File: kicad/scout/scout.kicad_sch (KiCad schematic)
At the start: 35 parts, among them J1 AudioJack2_SwitchT, J2 Conn_01x06_Male, J3 DIN5, J4 DIN5, SW26 SW_SPST, U1 ATmega328P-PU, U2 LM386, U3 6N138, Y1 16.00MHz

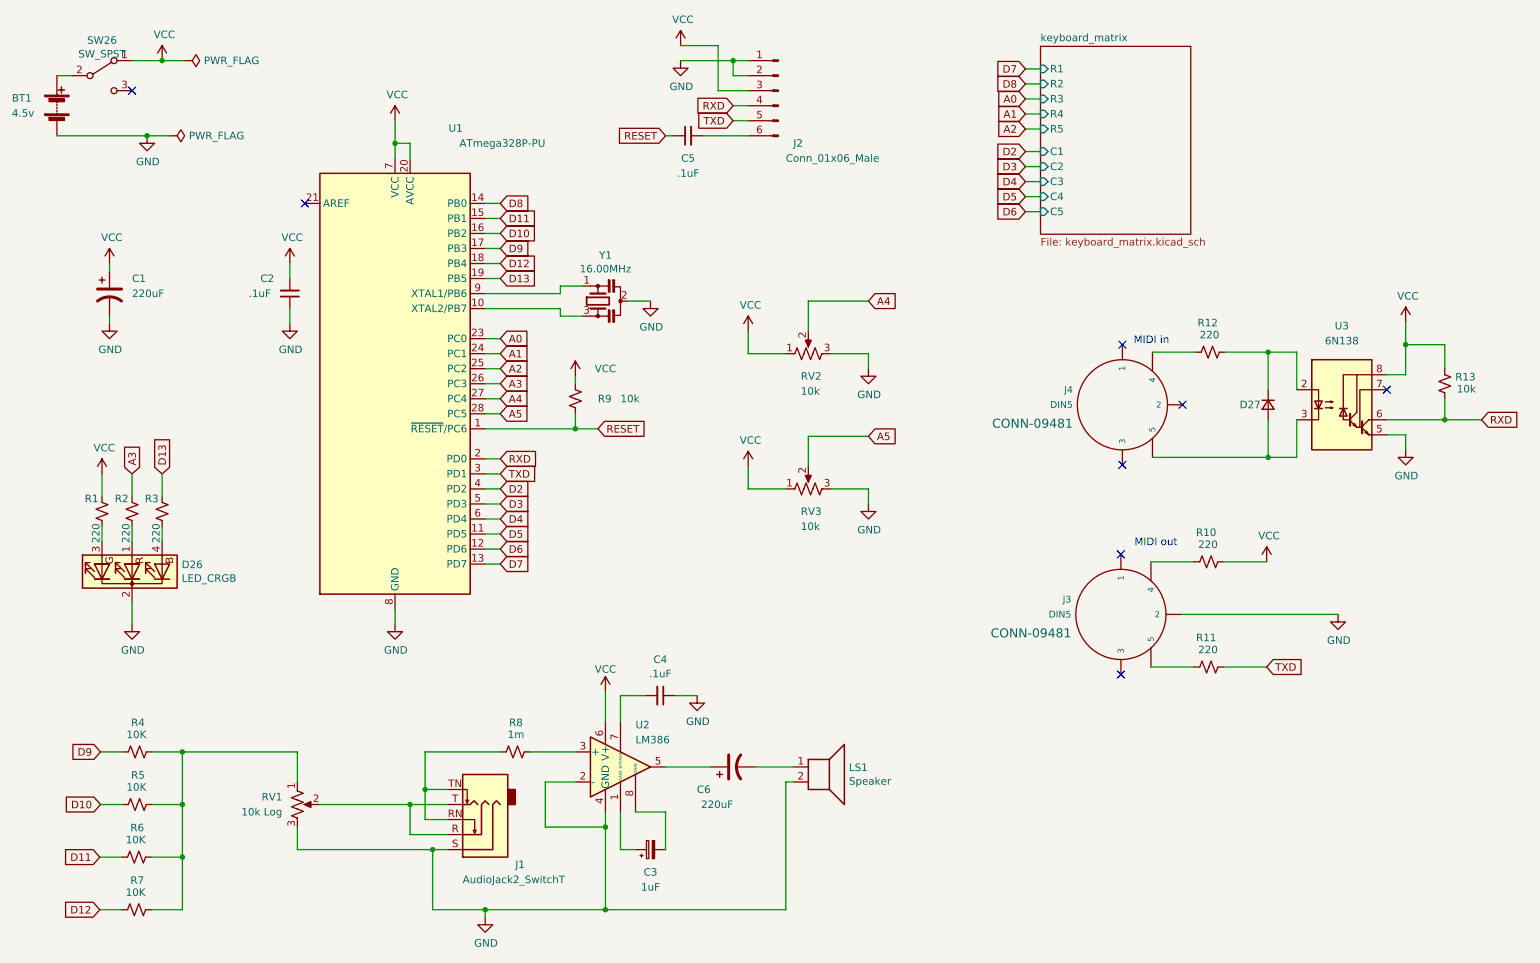
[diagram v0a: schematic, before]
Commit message: Update to latest kicad
No changes otherwise
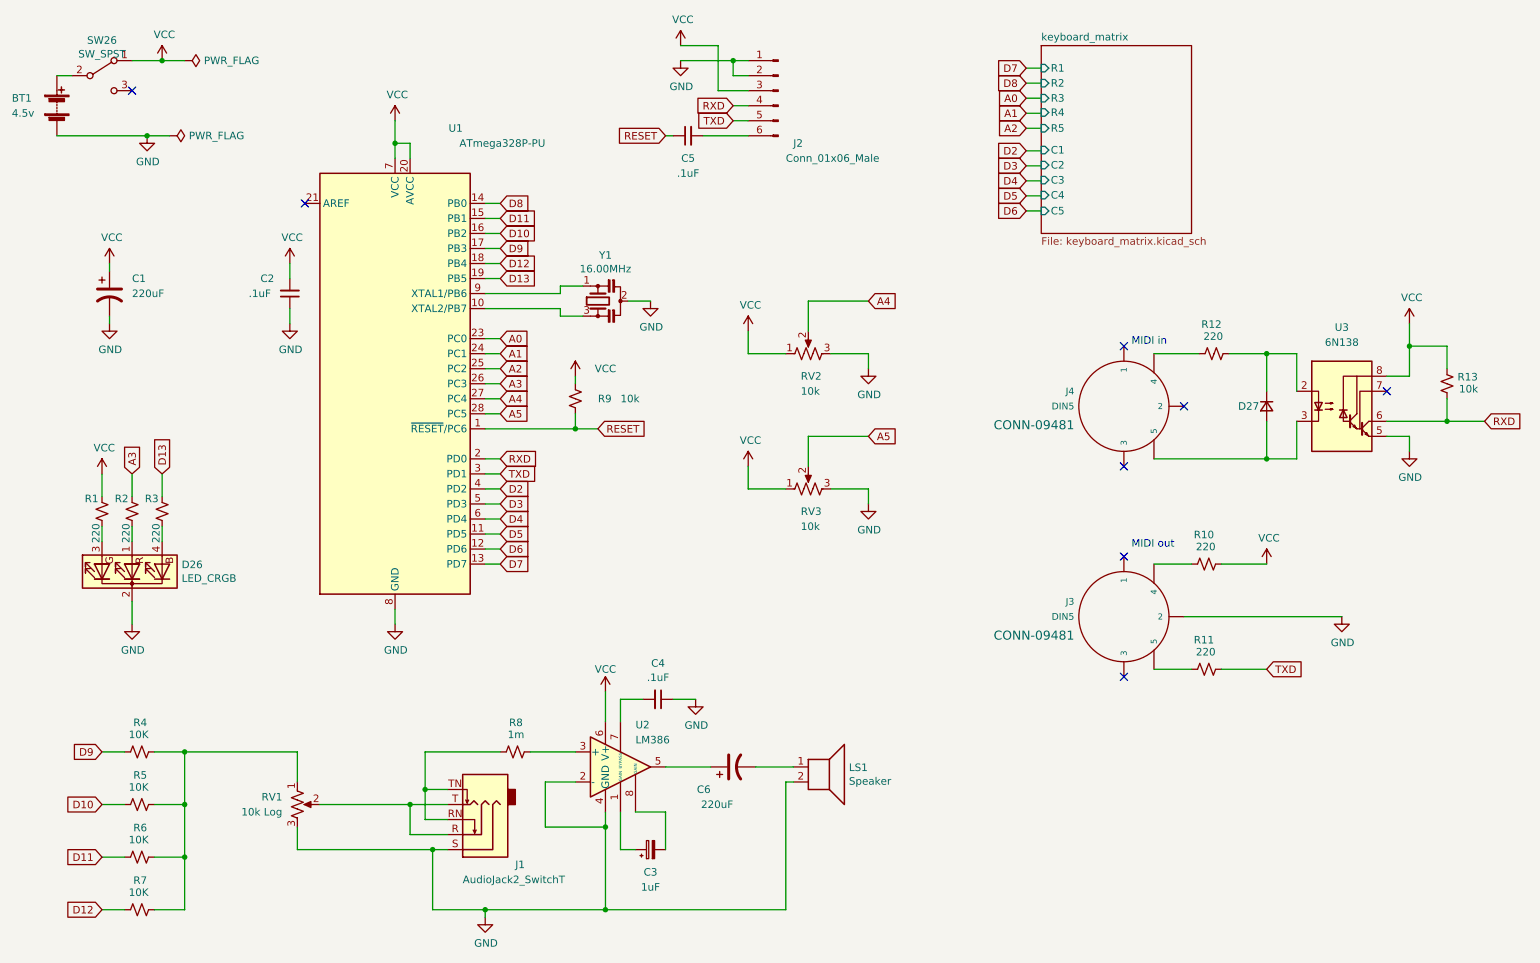
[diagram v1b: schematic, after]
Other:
- moved on the sheet: C4, J3, R10, R11, R12, R6, R7

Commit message: Update schematic
Should be no changes to function or PCB...

* Note pin assignments
* Tidy RV2 and RV3 voltage dividers
* Have MIDI read left to right
* Specify 1N4148 diodes

And add to readme
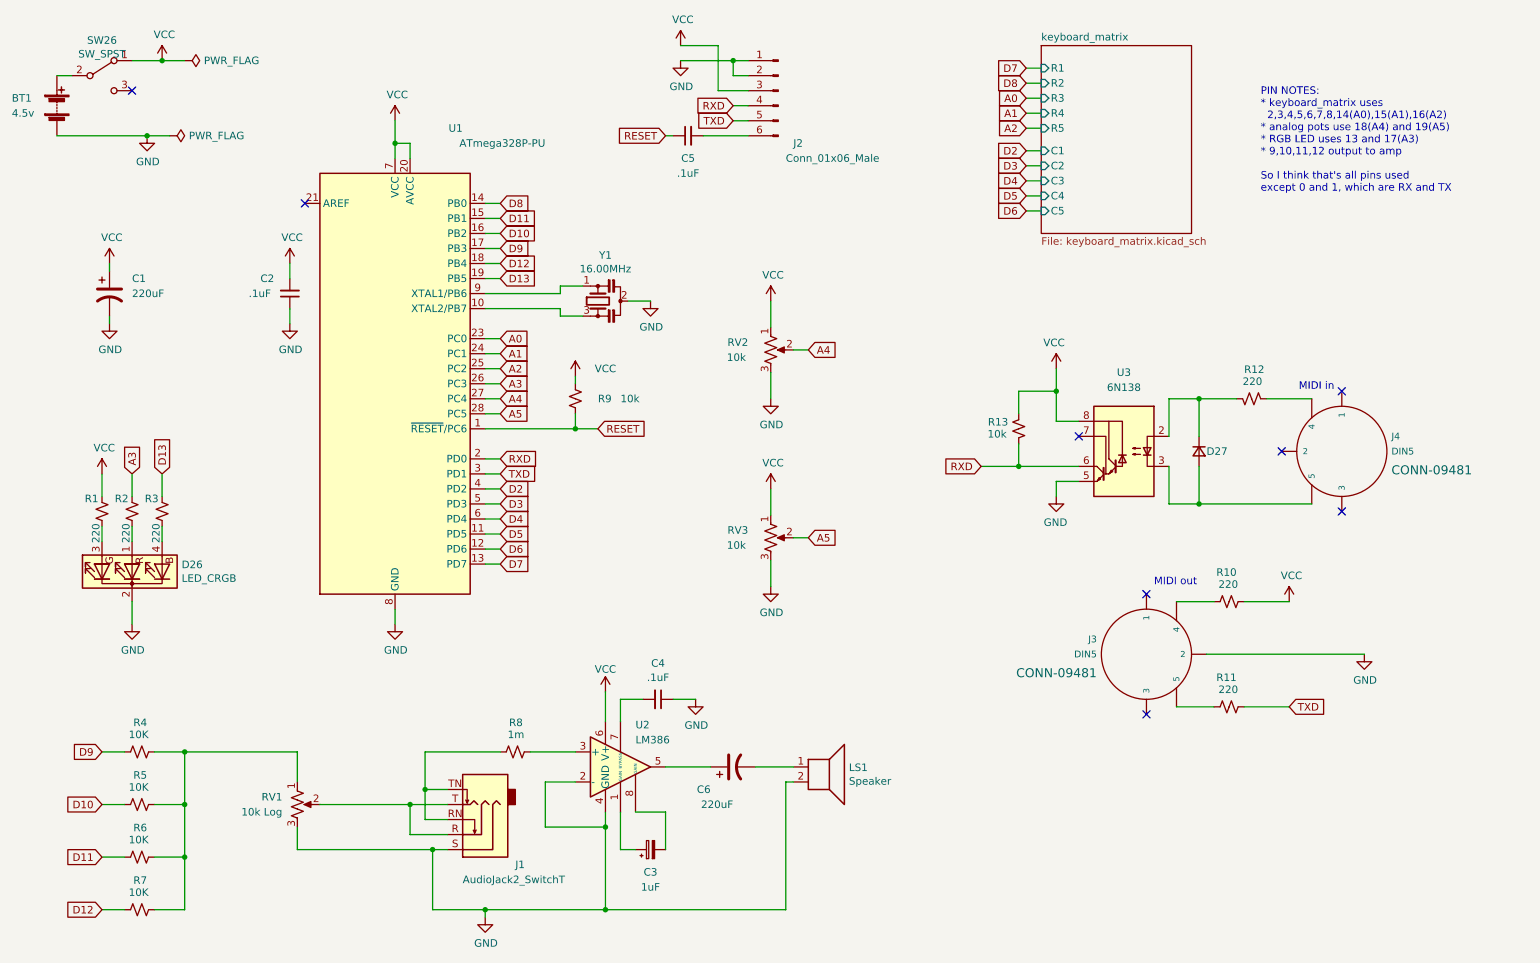
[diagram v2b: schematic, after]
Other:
- note added: "PIN NOTES: * keyboard_matrix uses 2,3,4,5,6,7,8,14(A0),15(A1),16(A2) * analog pots use 18(A4) and 19(A5) * RGB LED uses 13 and 17(A3) * 9,10,11,12 output to amp So I think that's all pins used except 0 and 1, which are RX and TX"
- moved on the sheet: D27, J3, J4, R10, R11, R12, R13, RV2, RV3, U3

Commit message: Try to reduce noise and other refinements
* Add decoupling cap before amp
* Add snubber circuit after amp
* Consider bass boost for next rev
* Self-document pin connection assignments in schematic
* Move branding text beyond key area
* Reverse power switch direction
* Enlarge UART hookup labels
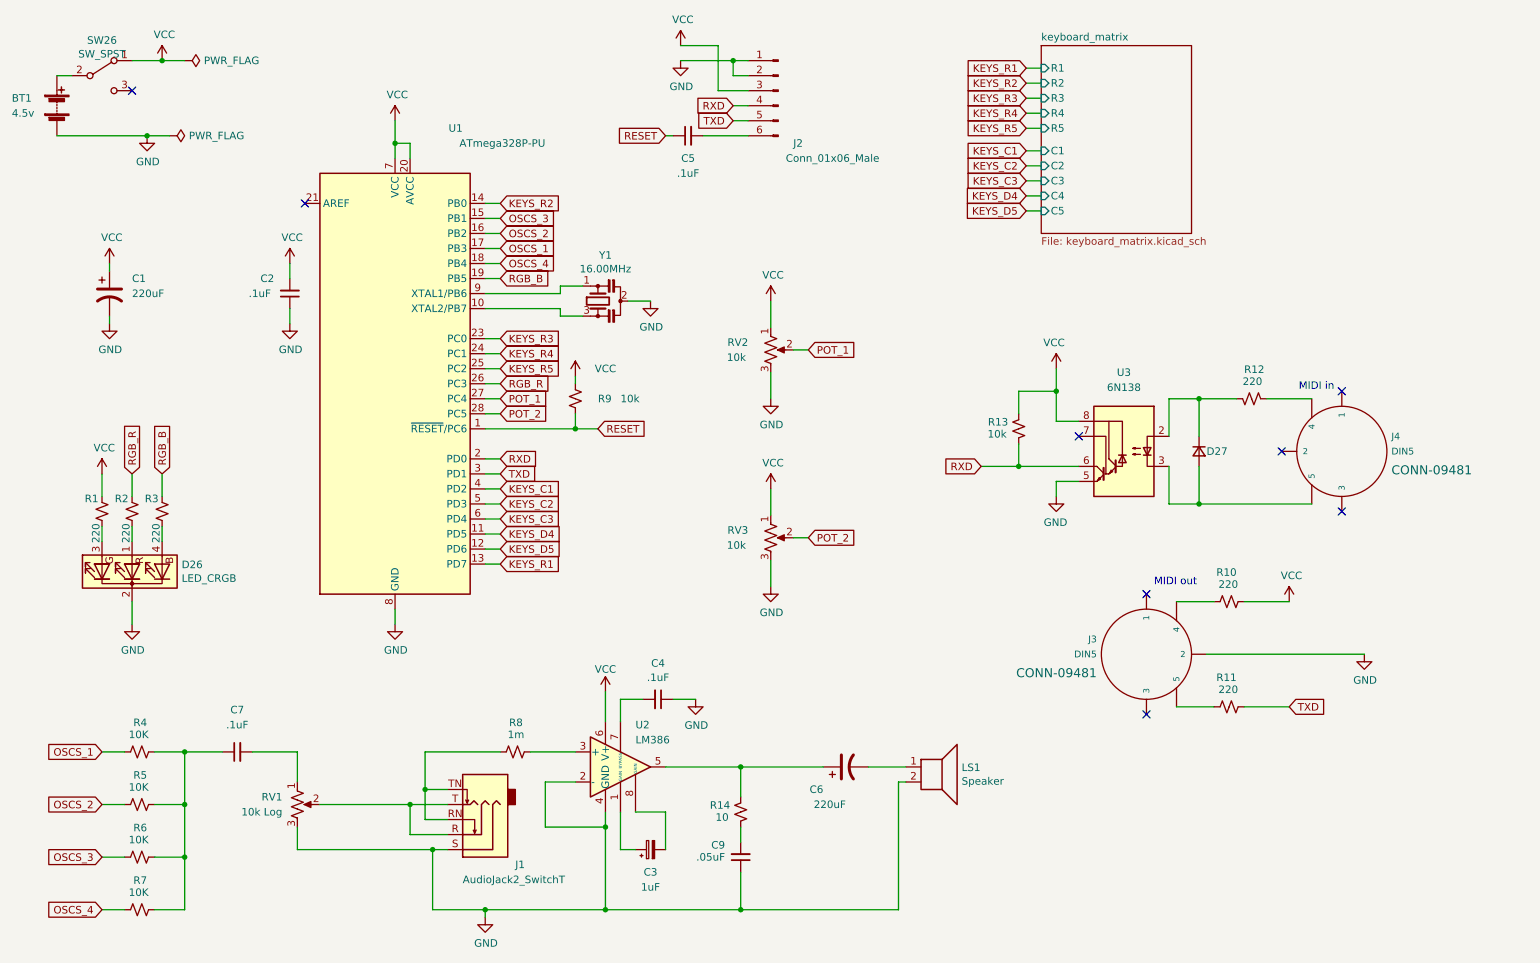
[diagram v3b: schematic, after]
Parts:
- added C7: .1uF, kicad-official/Capacitor_THT.pretty:C_Disc_D5.0mm_W2.5mm_P5.00mm, symbol Device:C_Small
- added C9: .05uF, kicad-official/Capacitor_THT.pretty:C_Disc_D5.0mm_W2.5mm_P5.00mm, symbol Device:C_Small
- added R14: 10, kicad-official/Resistor_THT.pretty:R_Axial_DIN0207_L6.3mm_D2.5mm_P10.16mm_Horizontal, symbol Device:R_Small_US
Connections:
- net GND: now also C9.1
- net at R4.2, R5.2, R6.2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: now also C7.1; no longer RV1.1
- net at C6.1, U2.5: now also R14.1
- net A0 renamed KEYS_R3
- net A1 renamed KEYS_R4
- net A2 renamed KEYS_R5
- net A3 renamed RGB_R
- net A4 renamed POT_1
- net A5 renamed POT_2
- net D10 renamed OSCS_2
- net D11 renamed OSCS_3
- net D12 renamed OSCS_4
- net D13 renamed RGB_B
- net D2 renamed KEYS_C1
- net D3 renamed KEYS_C2
- net D4 renamed KEYS_C3
- net D5 renamed KEYS_D4
- net D6 renamed KEYS_D5
- net D7 renamed KEYS_R1
- net D8 renamed KEYS_R2
- net D9 renamed OSCS_1
- new net: C7.2, RV1.1
- new net: C9.2, R14.2
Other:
- note removed: "PIN NOTES: * keyboard_matrix uses 2,3,4,5,6,7,8,14(A0),15(A1),16(A2) * analog pots use 18(A4) and 19(A5) * RGB LED uses 13 and 17(A3) * 9,10,11,12 output to amp So I think that's all pins used except 0 and 1, which are RX and TX"
- moved on the sheet: C6, LS1
